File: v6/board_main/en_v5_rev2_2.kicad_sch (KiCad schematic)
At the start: 34 parts, among them Q1 FDN302P, U1 REF3012AIDBZR, U2 MCP73833T-AMI/MF, U3 LTC3569EUDPBF

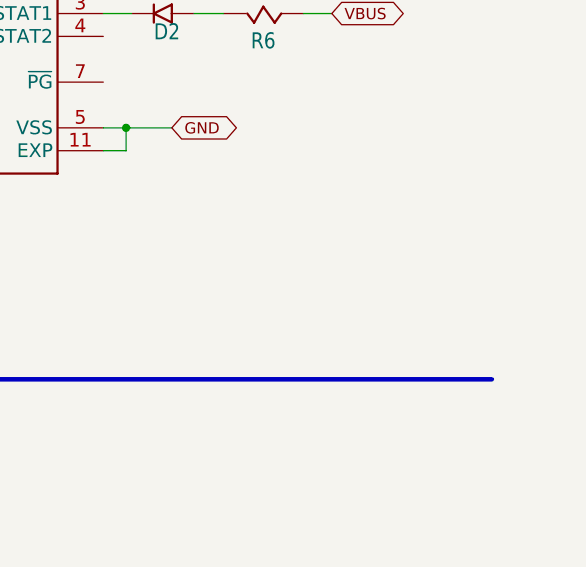
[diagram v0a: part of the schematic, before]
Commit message: Remove old artefacts and add mcu schematic to ENV6 main
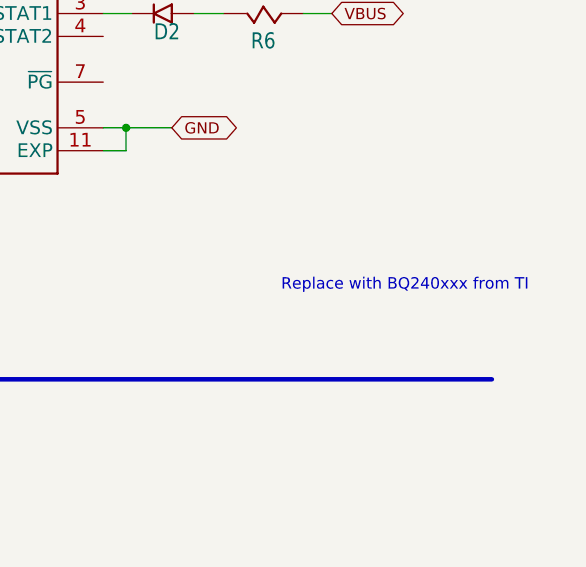
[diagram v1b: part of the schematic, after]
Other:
- note added: "Replace with BQ240xxx from TI"
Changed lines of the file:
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@@
+		)
+	)
+	(text "Replace with BQ240xxx from TI"
+		(exclude_from_sim no)
+		(at 264.668 88.646 0)
+		(effects
+			(font
+				(size 1.27 1.27)
+			)
 		)
 	)

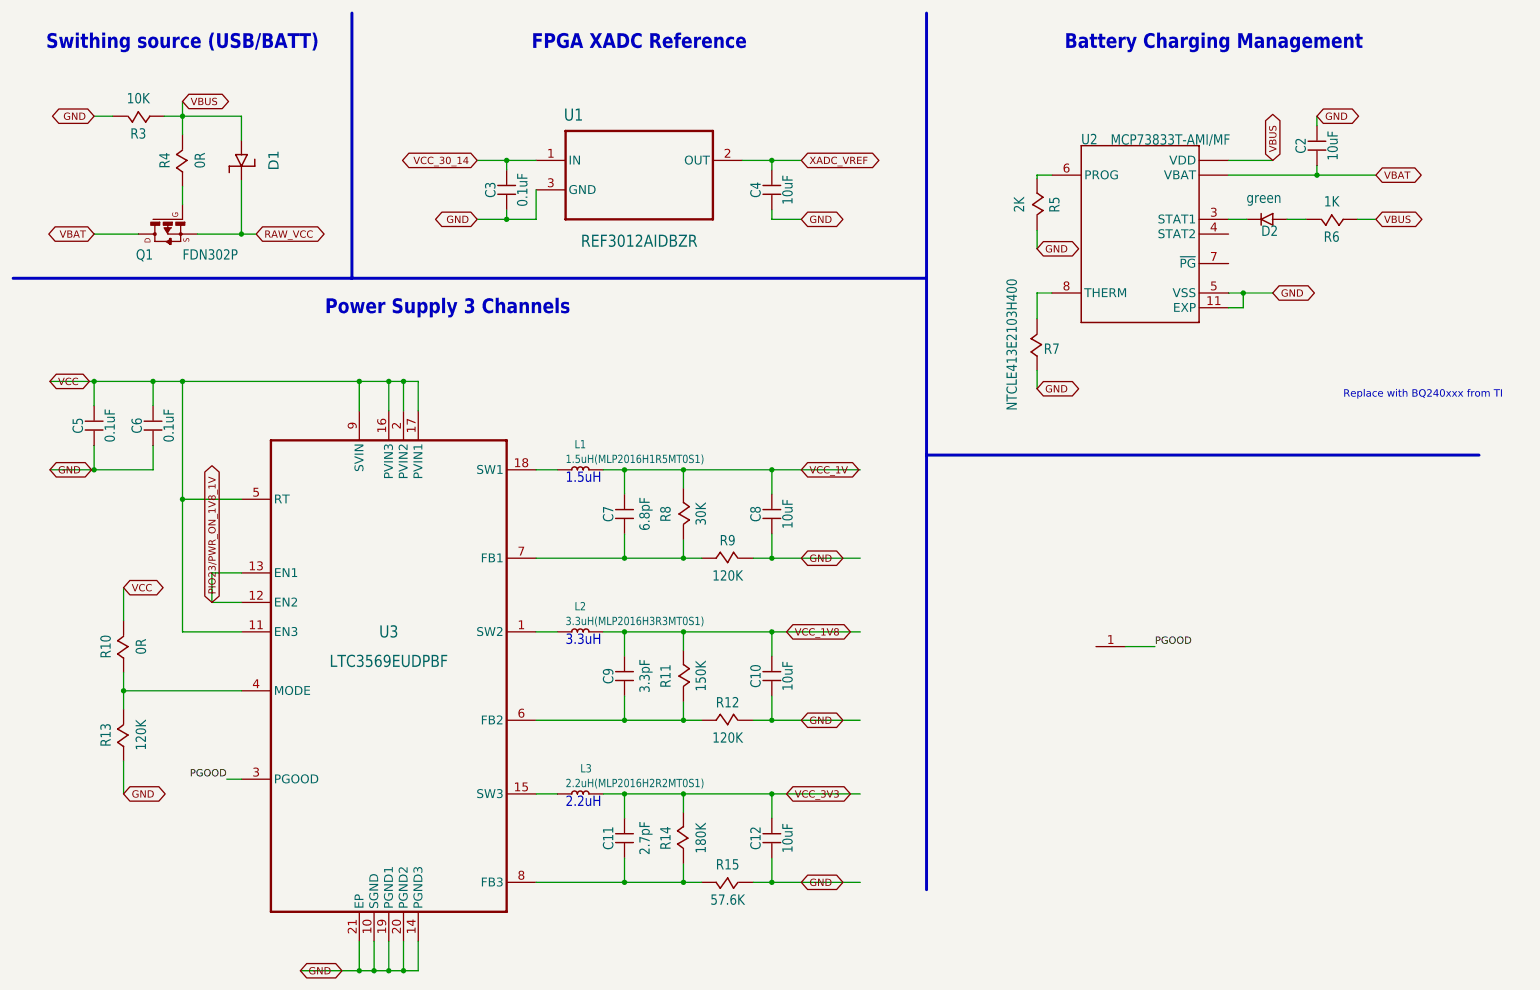
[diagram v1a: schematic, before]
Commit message: Rephrasing ENV5 design
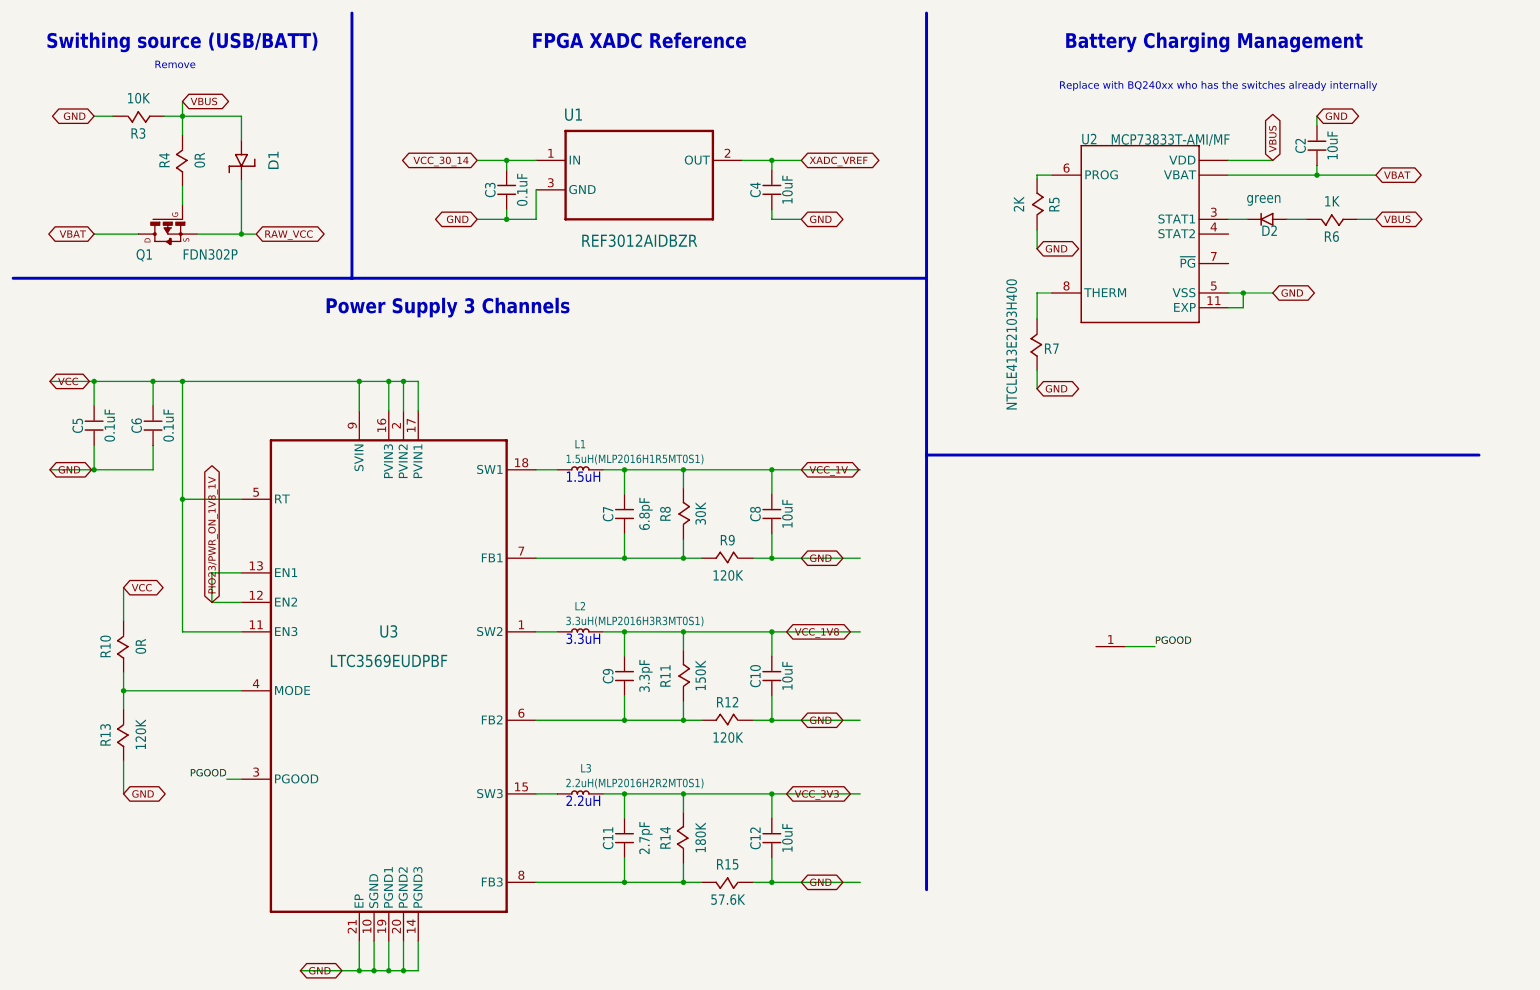
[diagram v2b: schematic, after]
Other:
- note added: "Remove"
- note added: "Replace with BQ240xx who has the switches already internally"
- note removed: "Replace with BQ240xxx from TI"
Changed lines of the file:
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@@
 	(generator_version "9.0")
 	(paper "User" 298.45 217.322)
+	(text "Replace with BQ240xx who has the switches already internally"
+		(exclude_from_sim no)
+		(at 229.362 35.56 0)
+		(effects
+			(font
+				(size 1.27 1.27)
+			)
+		)
+	)
 	(text "3.3uH"
 		(exclude_from_sim no)
@@
 			)
 			(justify left bottom)
-		)
-	)
-	(text "Replace with BQ240xxx from TI"
-		(exclude_from_sim no)
-		(at 264.668 88.646 0)
-		(effects
-			(font
-				(size 1.27 1.27)
-			)
 		)
 	)
@@
 			)
 		)
+	)
+	(text "Remove"
+		(exclude_from_sim no)
+		(at 49.53 32.004 0)
+		(effects
+			(font
+				(size 1.27 1.27)
+			)
+		)
